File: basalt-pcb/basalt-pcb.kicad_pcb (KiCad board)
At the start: 2 copper layers, 29 x 38 mm, 10 parts, among them J1 Conn_01x06_Pin, J2 Conn_01x06_Pin, J3 USB4215-03-A, U1 DI78L3.3ZAB, U2 STM32C071F8Px

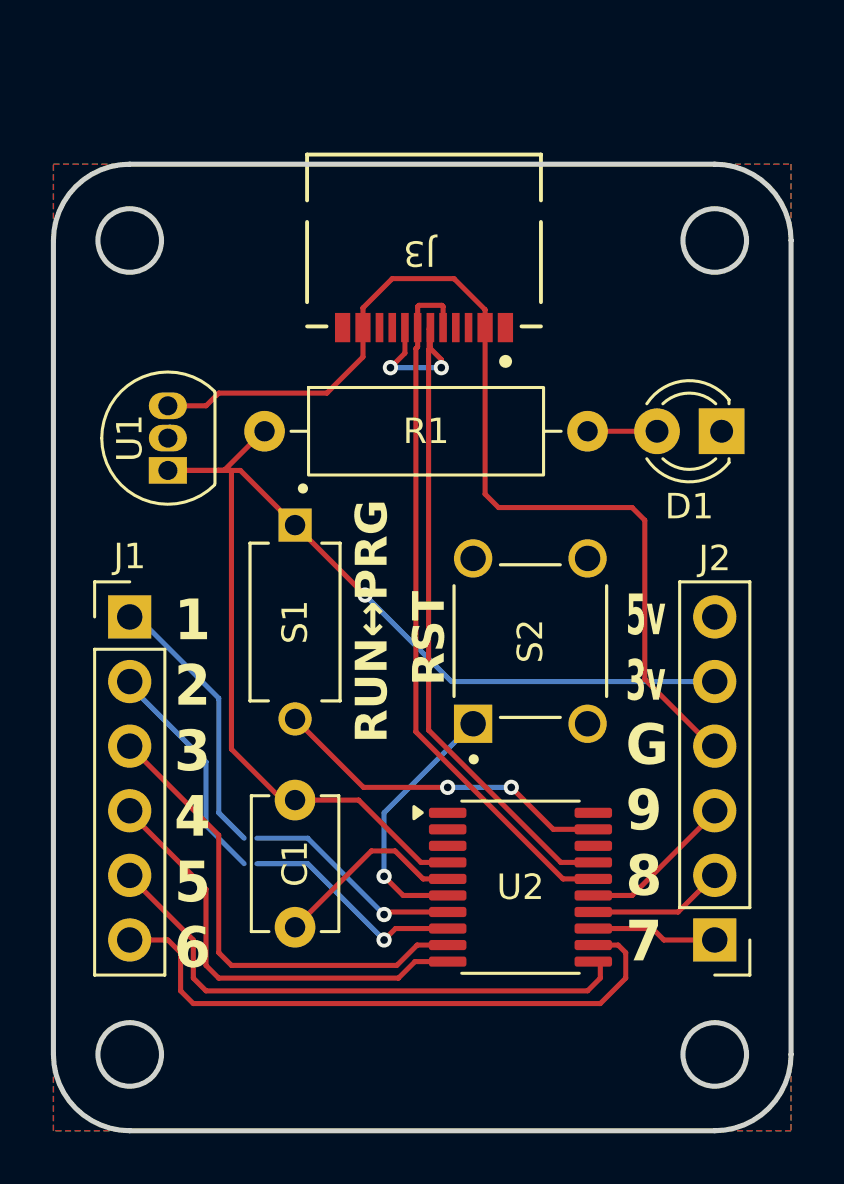
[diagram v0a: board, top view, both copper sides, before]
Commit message: Expose more pins, add ST-link pins at back, add diode to prevent backfeeding USB port
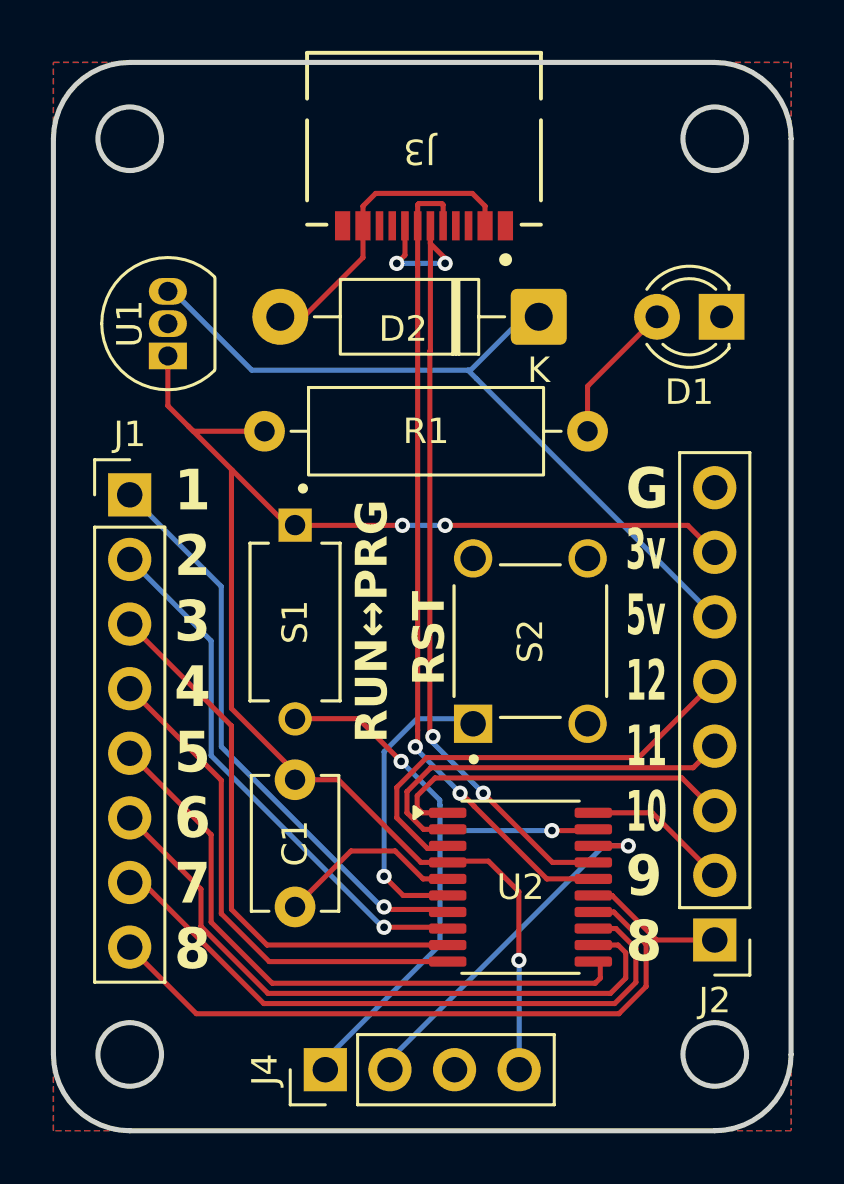
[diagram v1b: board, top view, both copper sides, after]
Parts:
- added D2: 1N5817, Diode_THT:D_DO-41_SOD81_P10.16mm_Horizontal, F.Cu at (154.1, 87.0)
- added J4: Conn_01x04_Pin, Connector_PinHeader_2.54mm:PinHeader_1x04_P2.54mm_Vertical, F.Cu at (145.7, 116.6)
- J1, J2: value Conn_01x06_Pin -> Conn_01x08_Pin; footprint Connector_PinHeader_2.54mm:PinHeader_1x06_P2.54mm_Vertical -> Connector_PinHeader_2.54mm:PinHeader_1x08_P2.54mm_Vertical
- moved J1 4.80 mm to (138.0, 94.0)
- moved D1 4.50 mm to (161.3, 87.0)
- moved U1 4.50 mm to (139.5, 88.5)
- moved J3 4.00 mm to (149.6, 80.0)
- moved C1 0.80 mm to (144.5, 105.2)
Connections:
- J2 pad 4: +5V -> Net-(J2-Pin_4)
- J2 pad 5: +3.3V -> Net-(J2-Pin_5)
- J2 pad 6: GND -> +5V
- J3 pad A4/B9: +5V -> Net-(D2-A)
- J3 pad B4/A9: +5V -> Net-(D2-A)
- U2 pad 1: unconnected-(U2-PB7/PB8-Pad1) -> Net-(J2-Pin_3)
- U2 pad 13: Net-(J2-Pin_1) -> Net-(J1-Pin_7)
- U2 pad 14: Net-(J2-Pin_2) -> Net-(J1-Pin_8)
- U2 pad 15: Net-(J2-Pin_3) -> Net-(J2-Pin_1)
- U2 pad 18: unconnected-(U2-PA13-Pad18) -> Net-(J4-Pin_2)
- U2 pad 2: unconnected-(U2-PC14-Pad2) -> Net-(J2-Pin_4)
- U2 pad 20: unconnected-(U2-PB3/PB4/PB5/PB6-Pad20) -> Net-(J2-Pin_2)
- U2 pad 3: unconnected-(U2-PC15-Pad3) -> Net-(J2-Pin_5)
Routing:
- net Net-(J1-Pin_8): track 0.00 -> 26.1 mm
- net Net-(J1-Pin_7): track 0.00 -> 25.6 mm
- net Net-(J2-Pin_5): track 0.00 -> 18.0 mm
- net Net-(J2-Pin_4): track 0.00 -> 15.7 mm
- net Net-(J4-Pin_2): track 0.00 -> 14.8 mm, vias 0 -> 1
- net Net-(J4-Pin_1): track 13.5 -> 25.8 mm
- net Net-(D2-A): track 0.00 -> 12.2 mm
- net +5V: track 40.2 -> 30.5 mm
- net +3.3V: track 51.4 -> 60.5 mm, vias 1 -> 3
- net Net-(J2-Pin_3): track 6.20 -> 14.5 mm
- net Net-(J3-DN1): track 28.0 -> 32.5 mm, vias 0 -> 2
- net Net-(J3-DP1): track 30.1 -> 33.9 mm, vias 2 -> 4
- net Net-(J1-Pin_1): track 19.5 -> 23.0 mm
- net Net-(J1-Pin_2): track 18.0 -> 21.2 mm
- net Net-(J1-Pin_3): track 19.1 -> 22.3 mm
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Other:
- board size 29 x 38 mm -> 29 x 42 mm
- board text added: "1 2 3 4 5 6 7 8"
- board text added: "3v 5v 12 11 10"
- board text added: "9 8"
- board text added: "G"
- board text removed: "1 2 3 4 5 6"
- board text removed: "5v 3v"
- board text removed: "G 9 8 7"

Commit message: Label additions and tweaks to pcb. Update sym/footprint.
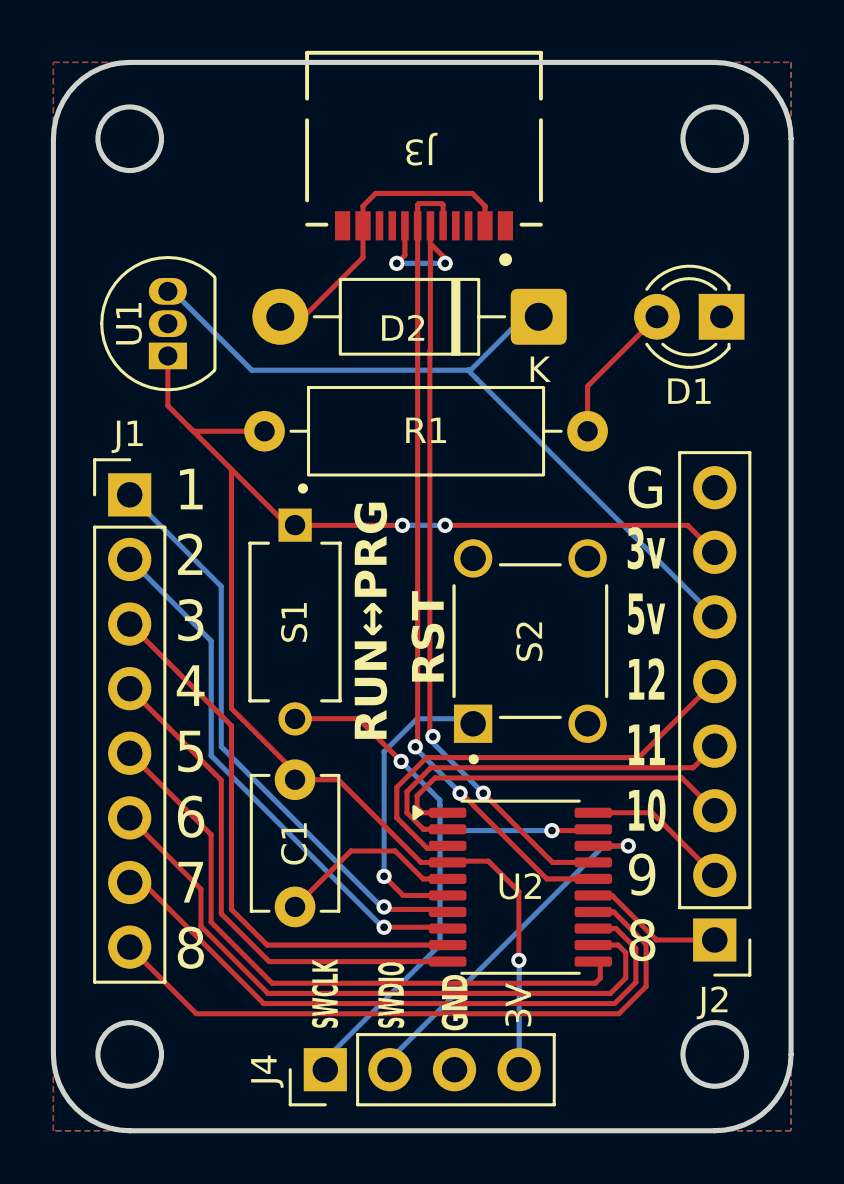
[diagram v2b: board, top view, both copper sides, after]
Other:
- board text added: "3V"
- board text added: "GND"
- board text added: "SWCLK"
- board text added: "SWDIO"
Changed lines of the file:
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@@
 		(layer "Edge.Cuts")
+	)
+	(gr_text "SWCLK"
+		(at 146.3 115 90)
+		(layer "F.SilkS")
+		(effects
+			(font
+				(size 1 0.5)
+				(thickness 0.125)
+				(bold yes)
+			)
+			(justify left bottom)
+		)
+	)
+	(gr_text "SWDIO\n"
+		(at 148.9 115 90)
+		(layer "F.SilkS")
+		(effects
+			(font
+				(size 1 0.5)
+				(thickness 0.125)
+				(bold yes)
+			)
+			(justify left bottom)
+		)
+	)
+	(gr_text "GND"
+		(at 151.4 115.1 90)
+		(layer "F.SilkS")
+		(effects
+			(font
+				(size 1 0.666)
+				(thickness 0.125)
+				(bold yes)
+			)
+			(justify left bottom)
+		)
 	)
 	(gr_text "3v\n5v\n12\n11\n10"
@@
 		)
 	)
+	(gr_text "3V"
+		(at 153.9 115 90)
+		(layer "F.SilkS")
+		(effects
+			(font
+				(size 1 1)
+				(thickness 0.125)
+			)
+			(justify left bottom)
+		)
+	)
 	(gr_text "RUN↔PRG"
 		(at 148.25 103.75 90)
@@
 			(font
 				(size 1.25 1.25)
-				(thickness 0.25)
+				(thickness 0.2125)
 				(bold yes)
 			)
@@
 			(font
 				(size 1.25 1.25)
-				(thickness 0.25)
+				(thickness 0.2125)
 				(bold yes)
 			)
@@
 			(font
 				(size 1.6 1.5)
-				(thickness 0.3)
-				(bold yes)
+				(thickness 0.2125)
 			)
 			(justify left bottom)
@@
 			(font
 				(size 1.6 1.5)
-				(thickness 0.3)
-				(bold yes)
+				(thickness 0.2125)
 			)
 			(justify left bottom)
@@
 			(font
 				(size 1.6 1.5)
-				(thickness 0.3)
-				(bold yes)
+				(thickness 0.2125)
 			)
 			(justify left bottom)
